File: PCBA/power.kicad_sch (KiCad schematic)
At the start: 8 parts

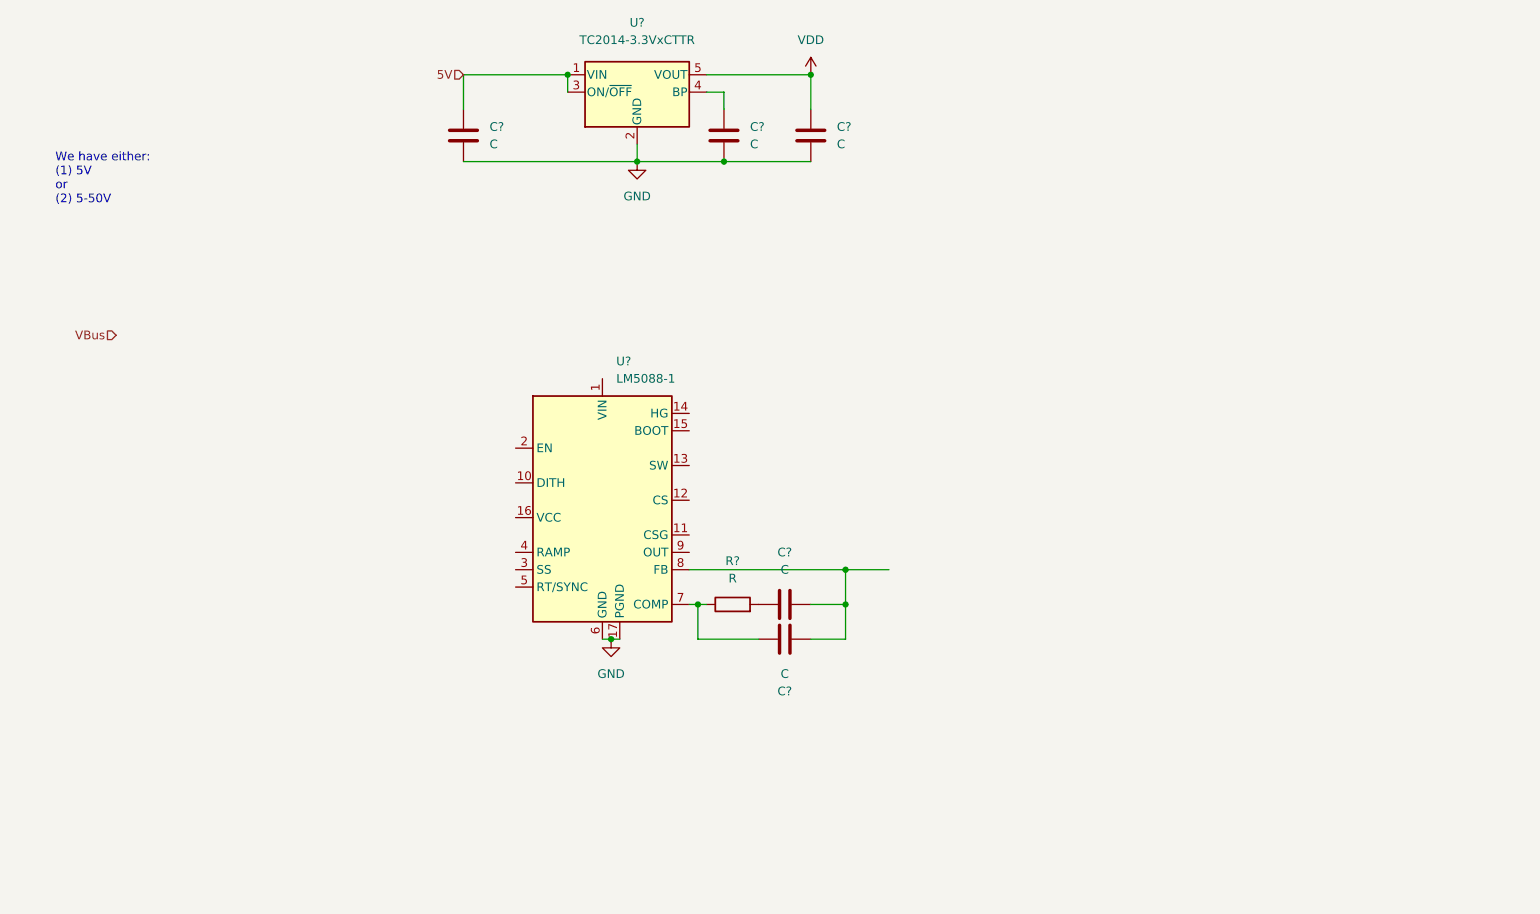
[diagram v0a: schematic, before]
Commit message: Adding DC/DC layout
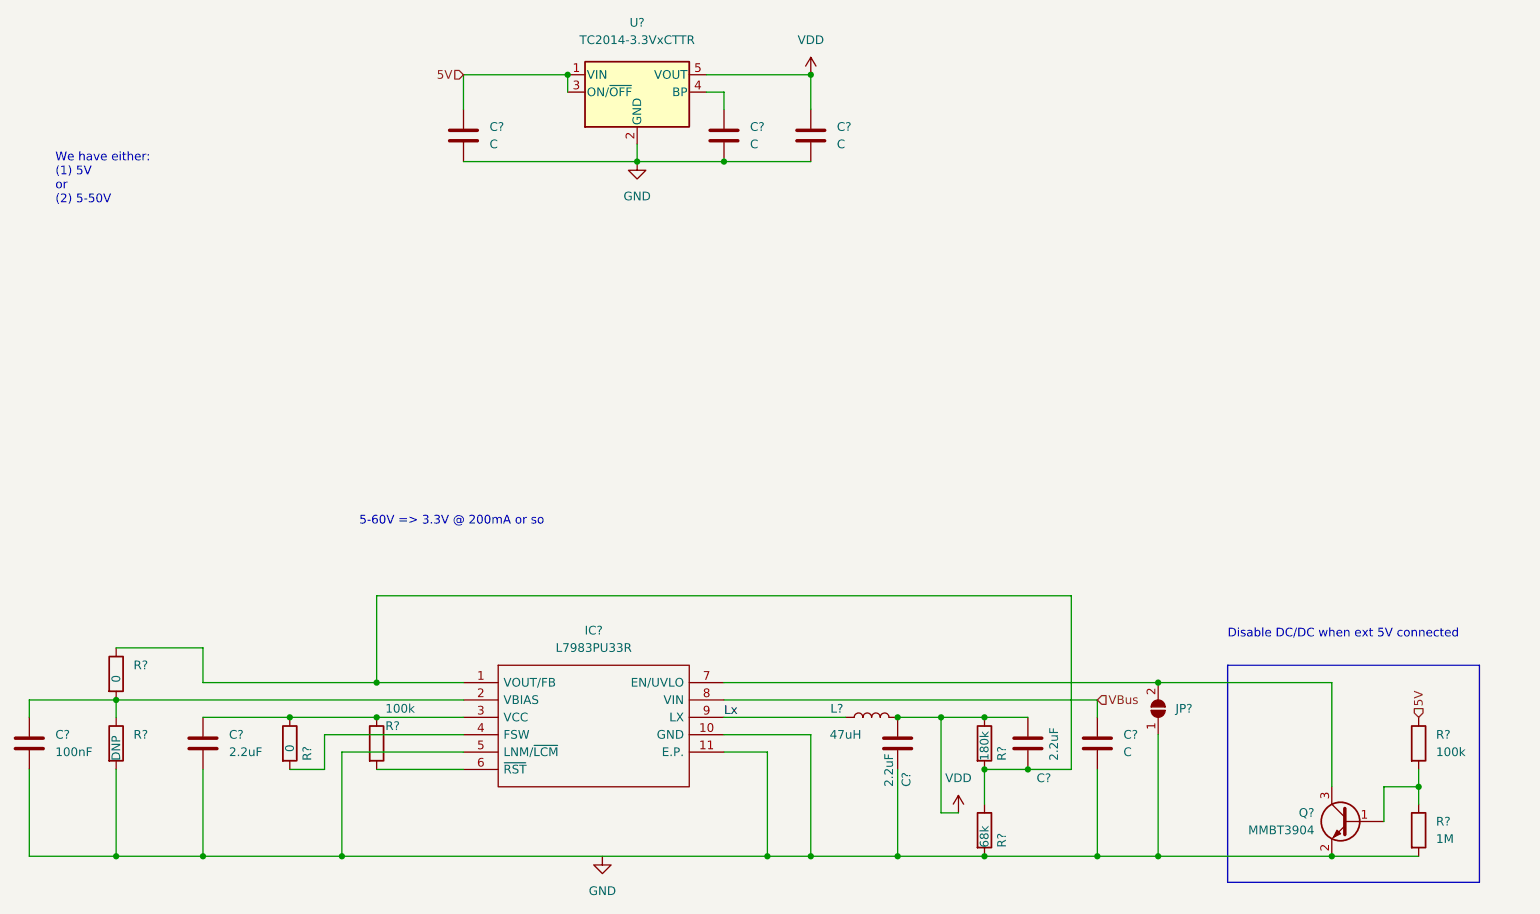
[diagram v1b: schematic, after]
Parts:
- removed C? (x2): C, symbol Device:C
- removed R?: R, symbol Device:R
- removed U?: LM5088-1, Package_SO:HTSSOP-16-1EP_4.4x5mm_P0.65mm_EP3.4x5mm_Mask3x3mm_ThermalVias, symbol Regulator_Switching:LM5088-1
- added C? (x3): 2.2uF, symbol Device:C
- added C?: C, symbol Device:C
- added C?: 100nF, symbol Device:C
- added IC?: L7983PU33R, L7983PU33R, symbol L7983PU33R:L7983PU33R
- added JP?: Disable, symbol Jumper:SolderJumper_2_Open
- added L?: 47uH, symbol Device:L
- added Q?: MMBT3904, Package_TO_SOT_SMD:SOT-23, symbol Transistor_BJT:MMBT3904
- added R? (x2): 100k, symbol Device:R
- added R?: 1M, symbol Device:R
- added R?: DNP, symbol Device:R
- added R?: 68k, symbol Device:R
- added R? (x2): 0, symbol Device:R
- added R?: 180k, symbol Device:R
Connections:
- net 5V: now also R?.1
- net VBus: now also C?.1, IC?.8 (VIN)
- net VDD: now also C?.1, C?.1, L?.2, R?.1
- new net: C?.2, IC?.1 (VOUT/FB), R?.1, R?.1, R?.2
- new net: C?.2, C?.2, C?.2, C?.2, IC?.10 (GND), IC?.11 (E.P.), IC?.5 (LNM/~{LCM}), JP?.1 (A), Q?.2 (E), R?.2, R?.2, R?.2
- new net: IC?.7 (EN/UVLO), JP?.2 (B), Q?.3 (C)
- new net: C?.1, IC?.3 (VCC), R?.1, R?.1
- new net: Q?.1 (B), R?.1, R?.2
- new net: C?.1, IC?.2 (VBIAS), R?.1, R?.2
- new net: IC?.4 (FSW), R?.2
- new net: IC?.6 (~{RST}), R?.2
- new net Lx: IC?.9 (LX), L?.1
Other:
- note added: "5-60V => 3.3V @ 200mA or so"
- note added: "Disable DC/DC when ext 5V connected"

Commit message: Add MP4560 schematic symbol+footprint
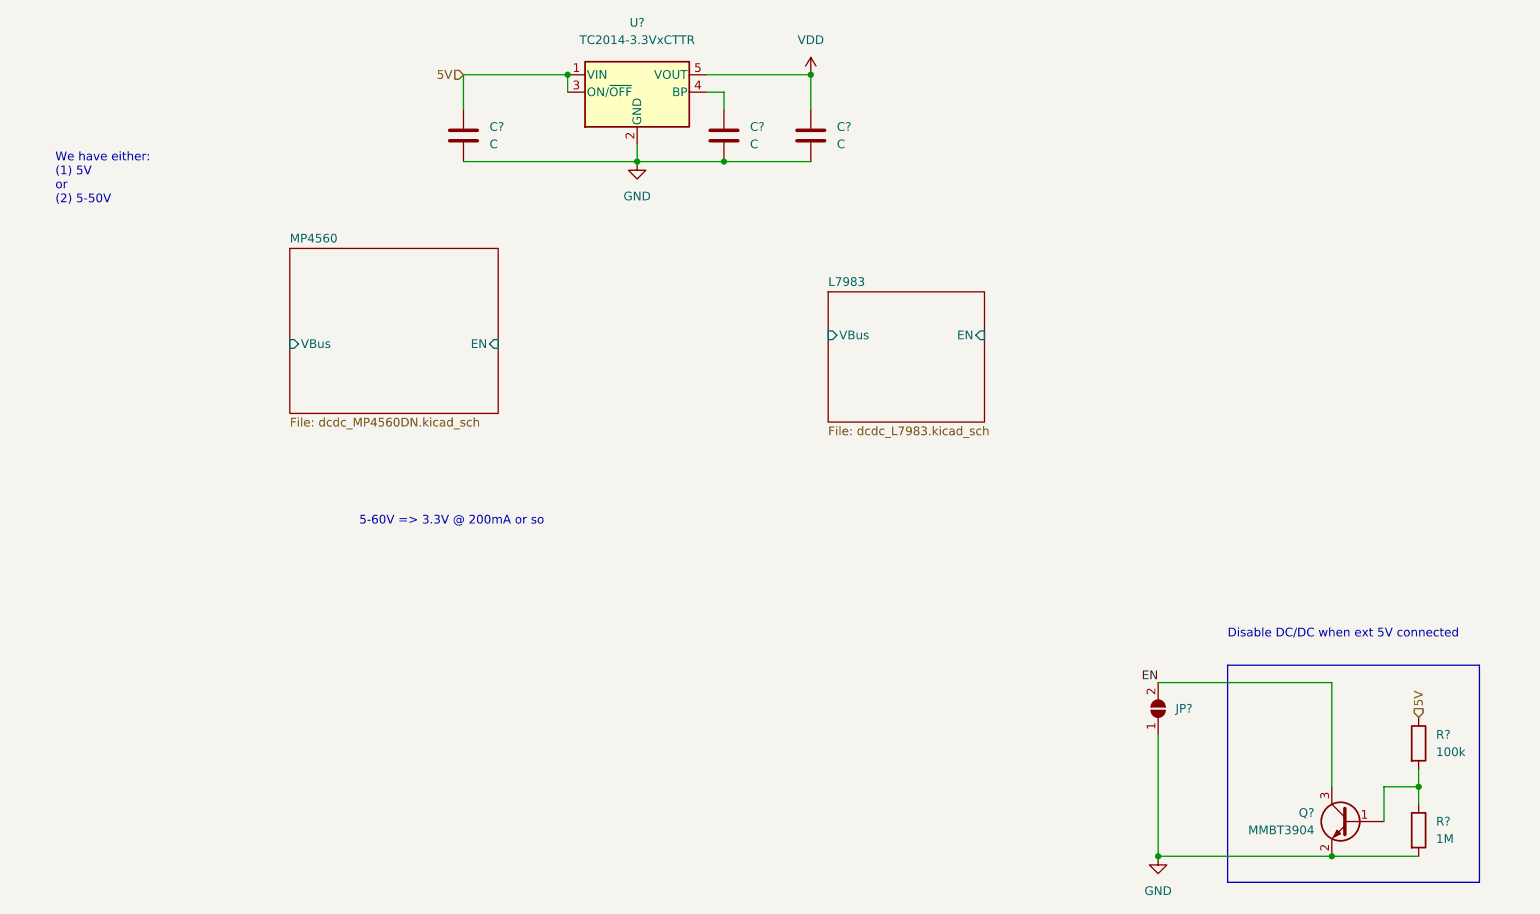
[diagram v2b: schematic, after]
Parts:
- removed C? (x3): 2.2uF, symbol Device:C
- removed C?: C, symbol Device:C
- removed C?: 100nF, symbol Device:C
- removed IC?: L7983PU33R, L7983PU33R, symbol L7983PU33R:L7983PU33R
- removed L?: 47uH, symbol Device:L
- removed R?: DNP, symbol Device:R
- removed R?: 68k, symbol Device:R
- removed R? (x2): 0, symbol Device:R
- removed R?: 100k, symbol Device:R
- removed R?: 180k, symbol Device:R
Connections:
- net GND: now also JP?.1 (A), Q?.2 (E), R?.2
- net EN: now reaches JP?.2 (B), Q?.3 (C)
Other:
- added sheet L7983 (dcdc_L7983.kicad_sch)
- added sheet MP4560 (dcdc_MP4560DN.kicad_sch)

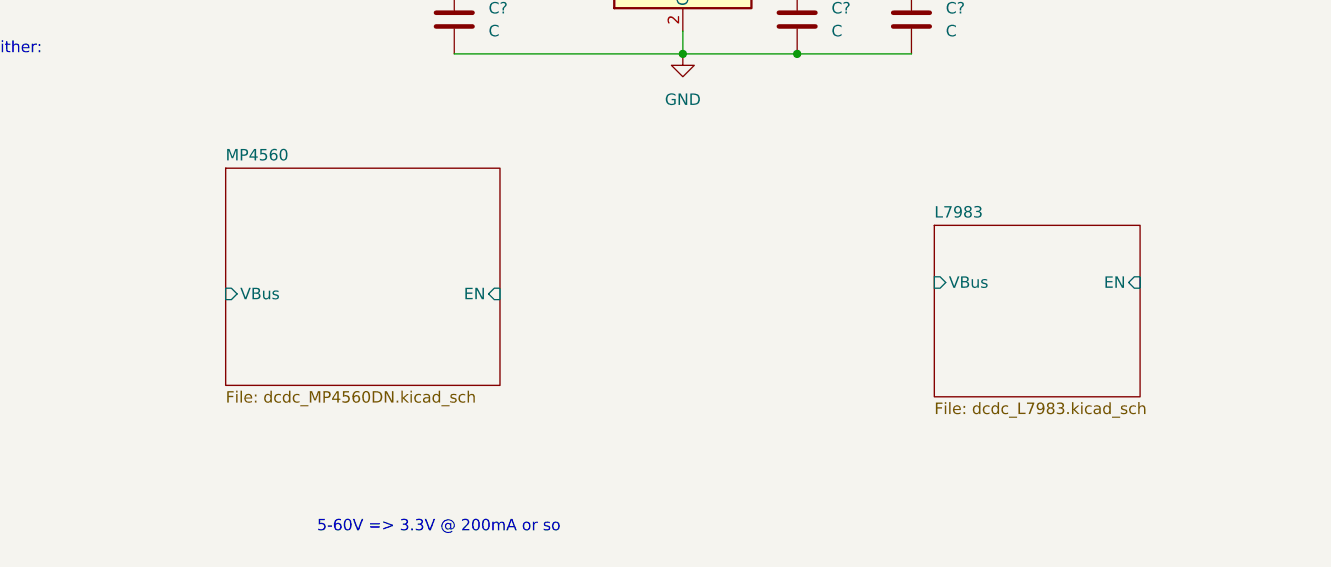
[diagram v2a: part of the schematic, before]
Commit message: Finish MP schematic
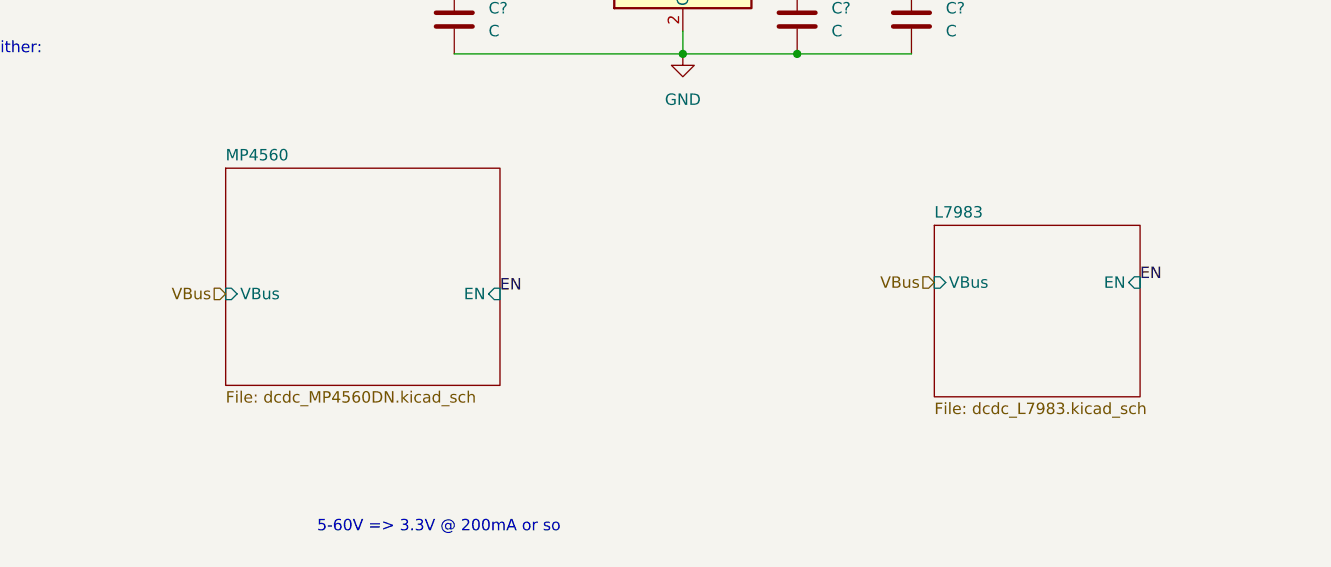
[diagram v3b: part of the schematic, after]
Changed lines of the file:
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@@
+    (effects (font (size 1.27 1.27)) (justify left bottom))
+  )
+  (label "EN" (at 132.08 64.77 0)
+    (effects (font (size 1.27 1.27)) (justify left bottom))
+  )
+  (label "EN" (at 203.2 63.5 0)
     (effects (font (size 1.27 1.27)) (justify left bottom))
   )
   (label "EN" (at 228.6 114.3 180)
     (effects (font (size 1.27 1.27)) (justify right bottom))
+  )
+  (hierarchical_label "VBus" (shape input) (at 101.6 64.77 180)
+    (effects (font (size 1.27 1.27)) (justify right))
   )
   (hierarchical_label "5V" (shape input) (at 266.7 119.38 90)
@@
     (effects (font (size 1.27 1.27)) (justify right))
   )
+  (hierarchical_label "VBus" (shape input) (at 180.34 63.5 180)
+    (effects (font (size 1.27 1.27)) (justify right))
+  )
